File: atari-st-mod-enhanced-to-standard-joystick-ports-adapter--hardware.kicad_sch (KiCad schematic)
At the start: 45 parts, among them J1 Joy0/Mouse, J2 Joy1, J3 OLED 128×64, J4 Enhanced Joystick Port, J5 Joy0/Mouse, J6 Joy1, Q1 1<Vgsth<2, Low Rdson, Vds >10, Q10 1<Vgsth<2, Low Rdson, Vds >10, Q2 1<Vgsth<2, Low Rdson, Vds >10, Q3 1<Vgsth<2, Low Rdson, Vds >10, Q4 1<Vgsth<2, Low Rdson, Vds >10, Q5 1<Vgsth<2, Low Rdson, Vds >10, Q6 1<Vgsth<2, Low Rdson, Vds >10, Q7 1<Vgsth<2, Low Rdson, Vds >10, Q8 1<Vgsth<2, Low Rdson, Vds >10, Q9 1<Vgsth<2, Low Rdson, Vds >10, SW1 Reset, SW2 Selector, SW3 Activate/Change, SW4 Cancel, U1 LM4040DBZ-3

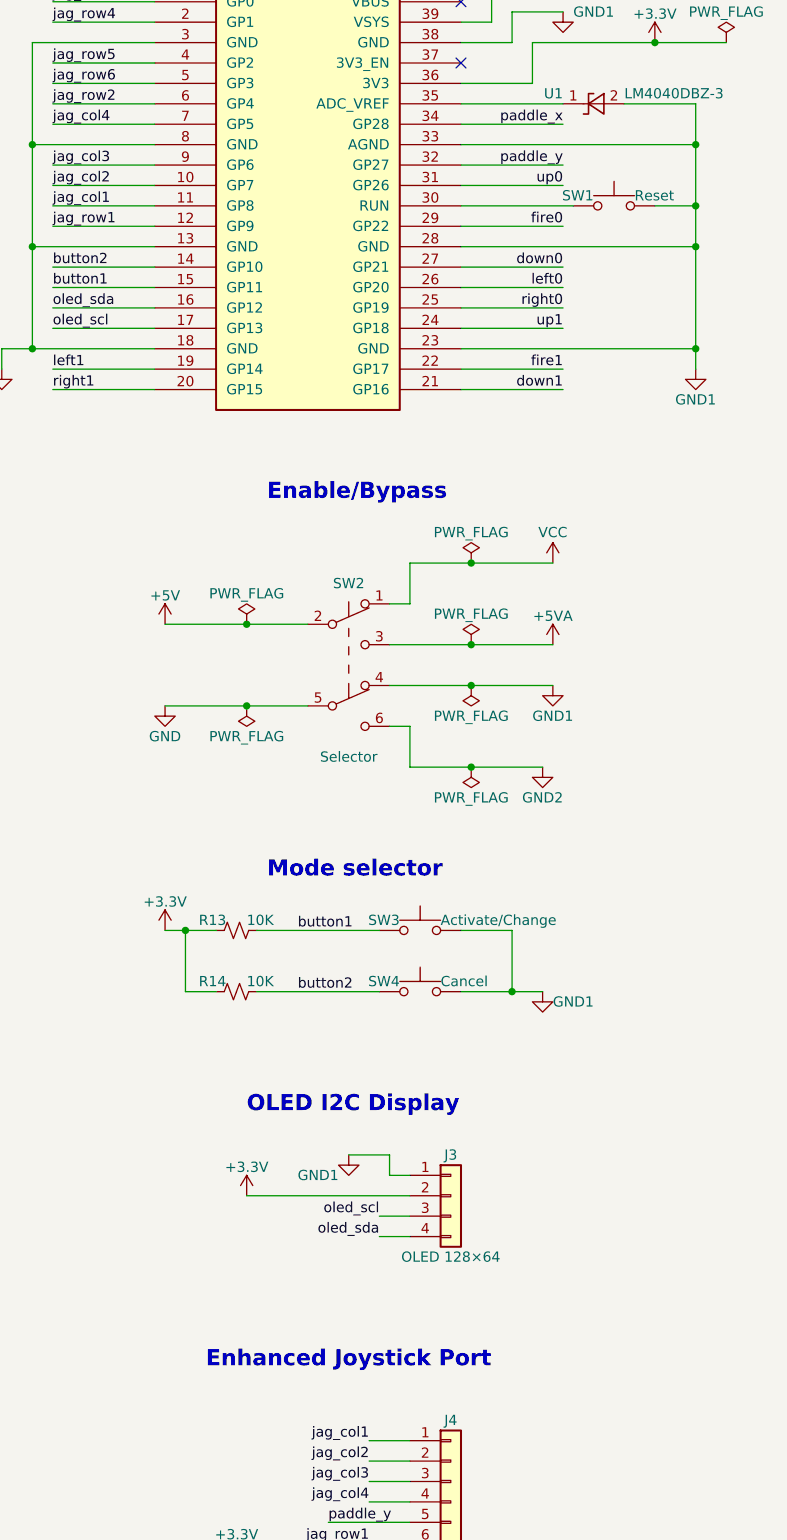
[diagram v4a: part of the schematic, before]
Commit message: add pull-up resistor to reset switch
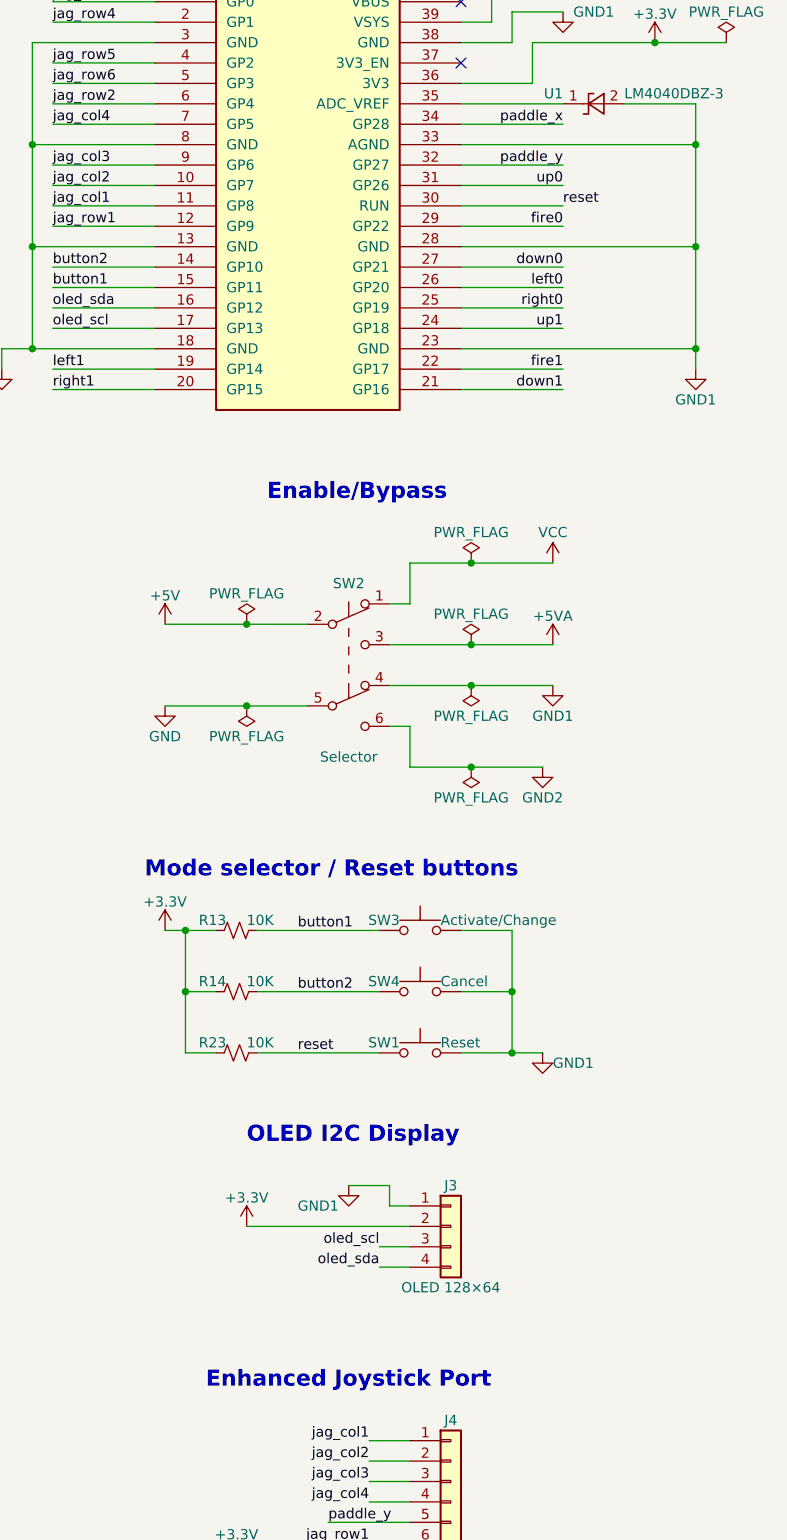
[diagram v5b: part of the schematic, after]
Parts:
- added R23: 10K, Resistor_SMD:R_0805_2012Metric, symbol Device:R_Small_US
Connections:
- net +3V3: now also R23.1
- net reset: now reaches A1.30 (RUN), SW1.1
- net reset: now also R23.2
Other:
- note added: "Mode selector / Reset buttons"
- note removed: "Mode selector"
- moved on the sheet: J3, SW1

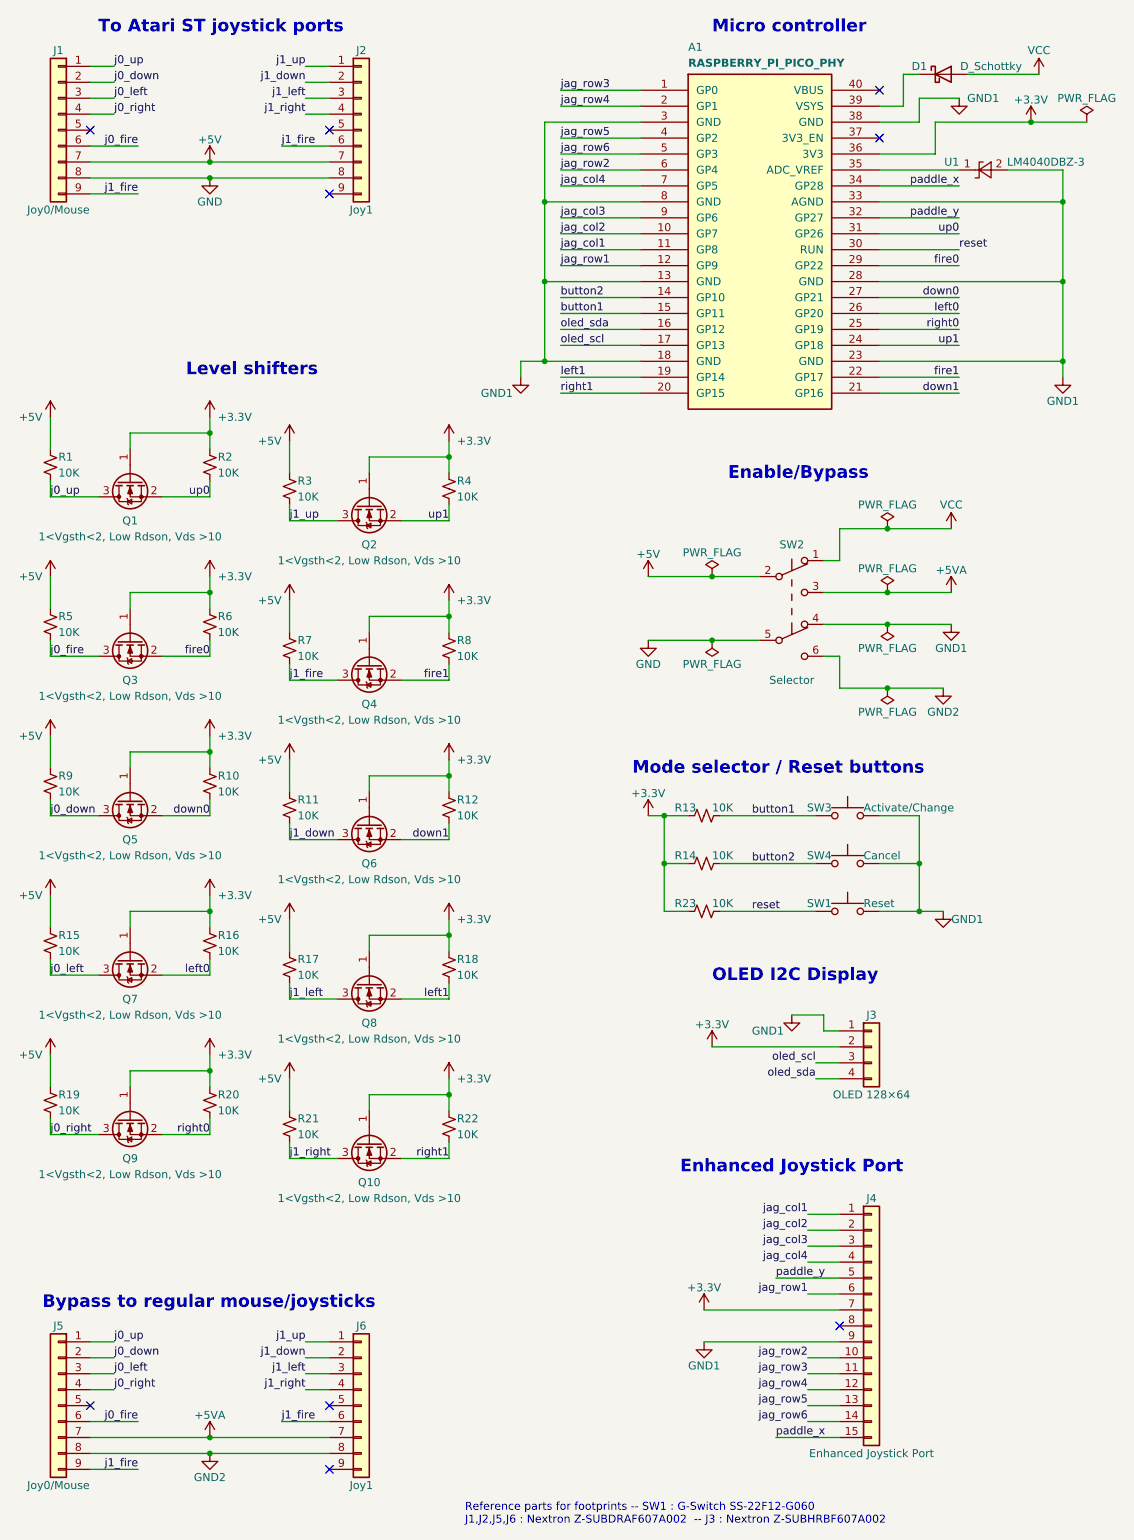
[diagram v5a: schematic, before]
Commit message: schematics : add mounting holes, shield pin 0 for connectors with metallic shields
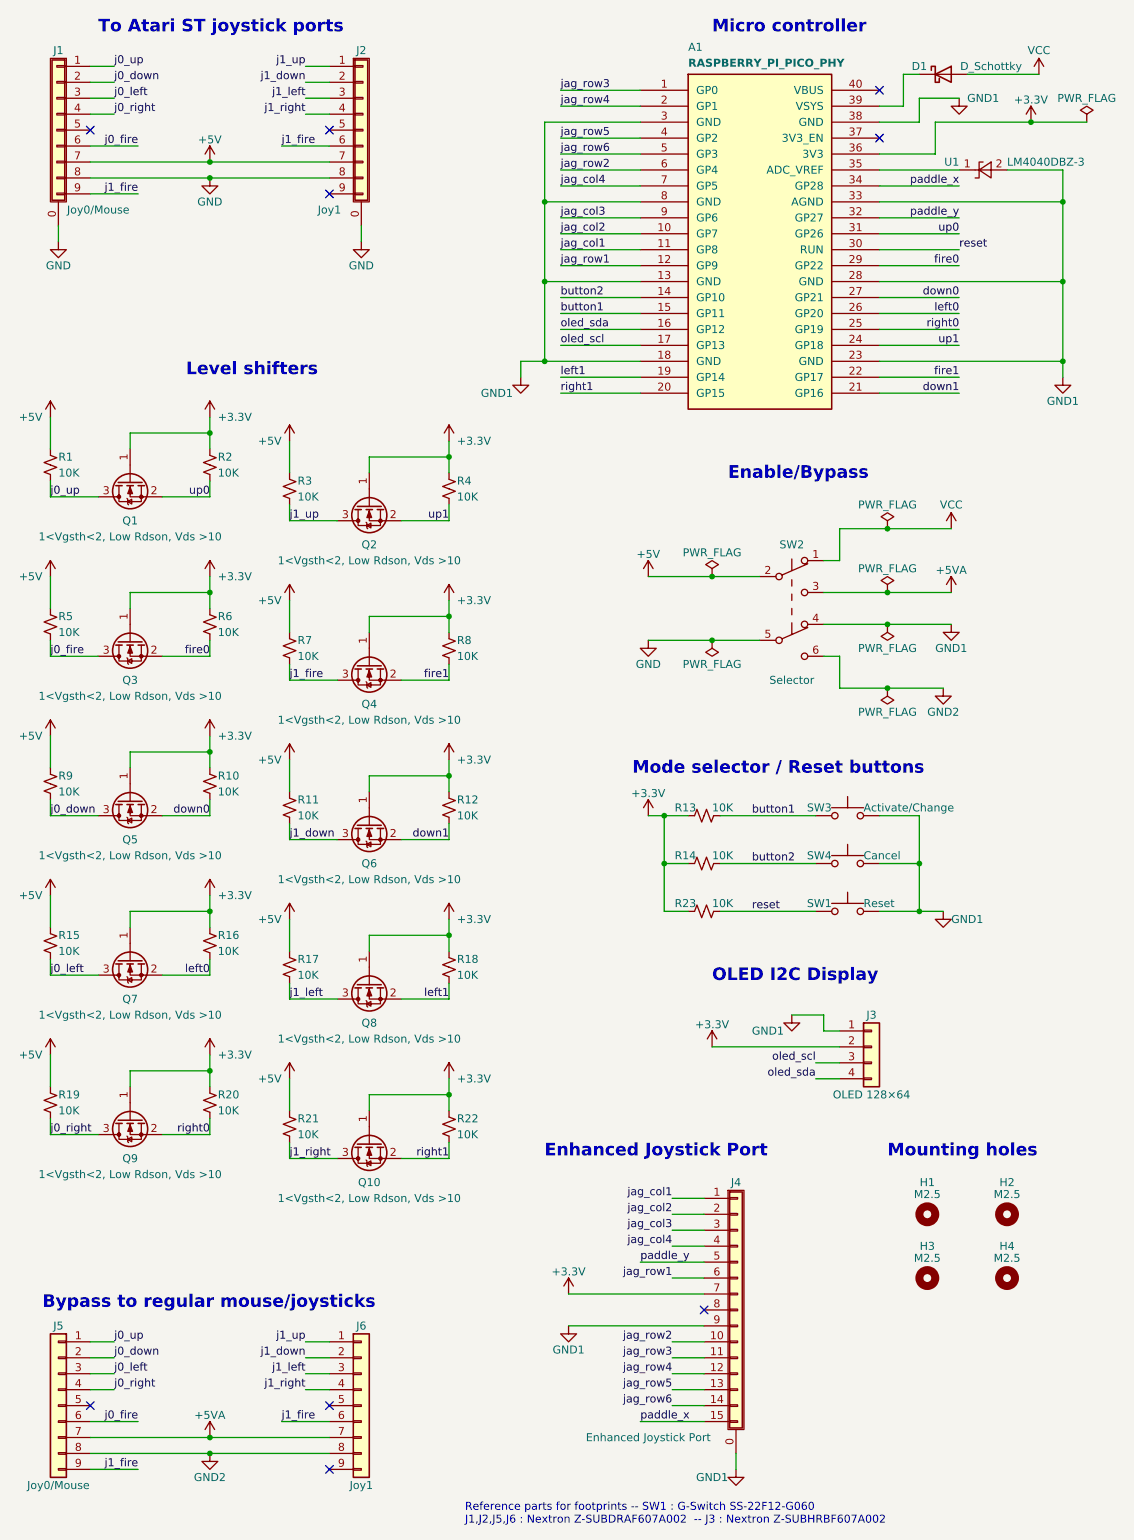
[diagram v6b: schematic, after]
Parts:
- added H1, H2, H3, H4: M2.5, MountingHole:MountingHole_2.7mm_M2.5, symbol Mechanical:MountingHole
- J1, J2: symbol Connector_Generic:Conn_01x09 -> Connector_Generic_Shielded:Conn_01x09_Shielded
- J4: symbol Connector_Generic:Conn_01x15 -> Connector_Generic_Shielded:Conn_01x15_Shielded
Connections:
- net GND: now also J1.0 (Shield), J2.0 (Shield)
- net GND1: now also J4.0 (Shield)
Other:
- note added: "Mounting holes"
